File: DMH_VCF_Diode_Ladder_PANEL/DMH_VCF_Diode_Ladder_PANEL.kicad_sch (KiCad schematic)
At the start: 5 parts, among them J0 Panel_GND_Solder_Wire_Pad

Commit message: Designed front panel
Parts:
- added H10: Drive, SynthStuff:Pot_Cutout_Medium, symbol SynthStuff:MountingHole_Pot
- added H11: Resonance, SynthStuff:Pot_Cutout_Medium, symbol SynthStuff:MountingHole_Pot
- added H12: CV 1 Amount, SynthStuff:Pot_Cutout_Tiny, symbol SynthStuff:MountingHole_Pot
- added H13: CV 2 Amount, SynthStuff:Pot_Cutout_Tiny, symbol SynthStuff:MountingHole_Pot
- added H14: LP, SynthStuff:Toggle_Switch_Cutout, symbol SynthStuff:MountingHole_ToggleSwitch
- added H15: BP, SynthStuff:Toggle_Switch_Cutout, symbol SynthStuff:MountingHole_ToggleSwitch
- added H16: HP, SynthStuff:Toggle_Switch_Cutout, symbol SynthStuff:MountingHole_ToggleSwitch
- added H5: Input, SynthStuff:Jack_6.35mm_Cutout_v3, symbol SynthStuff:MountingHole_Jack6.35mm_v2
- added H6: CV 1, SynthStuff:Jack_6.35mm_Cutout_v3, symbol SynthStuff:MountingHole_Jack6.35mm_v2
- added H7: CV 2, SynthStuff:Jack_6.35mm_Cutout_v3, symbol SynthStuff:MountingHole_Jack6.35mm_v2
- added H8: Output, SynthStuff:Jack_6.35mm_Cutout_Output_v6, symbol SynthStuff:MountingHole_Jack6.35mm_Output_v2
- added H9: Cutoff, SynthStuff:Pot_Cutout_Huge_v2, symbol SynthStuff:MountingHole_Pot
- J0: Function Panel GND -> GND
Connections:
- net GND: now also H10.1, H11.1, H12.1, H13.1, H14.1, H15.1, H16.1, H5.1, H6.1, H7.1, H8.1, H9.1

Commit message: Main schematic in progress
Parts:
- added H17: Bus CV Amount, SynthStuff:Pot_Cutout_Tiny, symbol SynthStuff:MountingHole_Pot
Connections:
- net GND: now also H17.1
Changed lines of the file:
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@@
+	)
+	(junction
+		(at 59.69 139.7)
+		(diameter 0)
+		(color 0 0 0 0)
 	)
 	(junction
@@
 	)
 	(junction
+		(at 76.2 114.3)
+		(diameter 0)
+		(color 0 0 0 0)
+	)
+	(junction
 		(at 27.94 269.24)
 		(diameter 0)
@@
 	(wire
 		(pts
+			(xy 59.69 114.3) (xy 59.69 139.7)
+		)
+		(stroke
+			(width 0)
+			(type default)
+		)
+	)
+	(wire
+		(pts
 			(xy 127 130.81) (xy 127 139.7)
 		)
@@
 	(wire
 		(pts
+			(xy 101.6 130.81) (xy 101.6 139.7)
+		)
+		(stroke
+			(width 0)
+			(type default)
+		)
+	)
+	(wire
+		(pts
 			(xy 33.02 269.24) (xy 33.02 273.05)
 		)
@@
 	(wire
 		(pts
+			(xy 76.2 114.3) (xy 59.69 114.3)
+		)
+		(stroke
+			(width 0)
+			(type default)
+		)
+	)
+	(wire
+		(pts
 			(xy 27.94 259.08) (xy 27.94 257.81)
 		)
@@
 		(pts
 			(xy 48.26 269.24) (xy 55.88 269.24)
-		)
-		(stroke
-			(width 0)
-			(type default)
-		)
-	)
-	(wire
-		(pts
-			(xy 101.6 114.3) (xy 101.6 139.7)
 		)
 		(stroke
@@
 					(unit 1)
 				)
+			)
+		)
+	)
+	(symbol
+		(lib_id "SynthStuff:MountingHole_Pot")
+		(at 101.6 128.27 0)
+		(unit 1)
+		(exclude_from_sim yes)
+		(in_bom no)
+		(on_board yes)
+		(dnp no)
+		(fields_autoplaced yes)
+		(property "Reference" "H17"
+			(at 104.14 124.4599 0)
+			(effects
+				(font
+					(size 1.27 1.27)
+				)
+				(justify left)
+			)
+		)
+		(property "Value" "Bus CV Amount"
+			(at 104.14 126.9999 0)
+			(effects
+				(font
+					(size 1.27 1.27)
+				)
+				(justify left)
+			)
+		)
+		(property "Footprint" "SynthStuff:Pot_Cutout_Tiny"
+			(at 101.6 128.27 0)
+			(effects
+				(font
+					(size 1.27 1.27)
+				)
+				(hide yes)
+			)
+		)
+		(property "Datasheet" "~"
+			(at 101.6 128.27 0)
+			(effects
+				(font
+					(size 1.27 1.27)
+				)
+				(hide yes)
+			)
+		)
+		(property "Description" "Pot Mounting Hole"
+			(at 104.14 129.5399 0)
+			(effects
+				(font
+					(size 1.27 1.27)
+				)
+				(justify left)
+			)
+		)
+		(pin "1"
+		)
+		(instances
+			(project "DMH_VCF_Diode_Ladder_PANEL"
+				(path "/a552705f-a9fe-462e-9913-5cfcc08b233c"
+					(reference "H17")
+					(unit 1)
+				)

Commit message: Finished schematic and added Bus CV 2 pot
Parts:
- added H18: CV 2, SynthStuff:Jack_6.35mm_Cutout_v3, symbol SynthStuff:MountingHole_Jack6.35mm_v2
- H13: value CV 2 Amount -> CV 3 Amount
- H17: value Bus CV Amount -> (Bus) CV 2 Amount
- H7: value CV 2 -> CV 3
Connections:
- net GND: now also H18.1
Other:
- moved on the sheet: H5, H6, H7, H8
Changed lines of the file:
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@@
+	)
+	(junction
+		(at 73.66 181.61)
+		(diameter 0)
+		(color 0 0 0 0)
 	)
 	(junction
@@
 	(wire
 		(pts
+			(xy 97.79 181.61) (xy 76.2 181.61)
+		)
+		(stroke
+			(width 0)
+			(type default)
+		)
+	)
+	(wire
+		(pts
 			(xy 127 105.41) (xy 127 114.3)
 		)
@@
 	(wire
 		(pts
+			(xy 97.79 190.5) (xy 97.79 181.61)
+		)
+		(stroke
+			(width 0)
+			(type default)
+		)
+	)
+	(wire
+		(pts
 			(xy 101.6 139.7) (xy 101.6 146.05)
 		)
@@
 	(wire
 		(pts
-			(xy 135.89 190.5) (xy 135.89 181.61)
+			(xy 148.59 190.5) (xy 148.59 181.61)
 		)
 		(stroke
@@
 	(wire
 		(pts
+			(xy 73.66 181.61) (xy 76.2 181.61)
+		)
+		(stroke
+			(width 0)
+			(type default)
+		)
+	)
+	(wire
+		(pts
 			(xy 101.6 92.71) (xy 101.6 114.3)
 		)
@@
 	(wire
 		(pts
+			(xy 148.59 181.61) (xy 135.89 181.61)
+		)
+		(stroke
+			(width 0)
+			(type default)
+		)
+	)
+	(wire
+		(pts
 			(xy 59.69 181.61) (xy 59.69 171.45)
 		)
@@
 	(wire
 		(pts
-			(xy 76.2 181.61) (xy 85.09 181.61)
-		)
-		(stroke
-			(width 0)
-			(type default)
-		)
-	)
-	(wire
-		(pts
 			(xy 55.88 257.81) (xy 55.88 259.08)
 		)
@@
 	(wire
 		(pts
-			(xy 59.69 190.5) (xy 59.69 181.61)
+			(xy 48.26 190.5) (xy 48.26 181.61)
 		)
 		(stroke
@@
 	(wire
 		(pts
-			(xy 110.49 190.5) (xy 110.49 181.61)
+			(xy 123.19 190.5) (xy 123.19 181.61)
 		)
 		(stroke
@@
 	(wire
 		(pts
-			(xy 59.69 181.61) (xy 76.2 181.61)
-		)
-		(stroke
-			(width 0)
-			(type default)
-		)
-	)
-	(wire
-		(pts
-			(xy 110.49 181.61) (xy 135.89 181.61)
+			(xy 59.69 181.61) (xy 73.66 181.61)
+		)
+		(stroke
+			(width 0)
+			(type default)
+		)
+	)
+	(wire
+		(pts
+			(xy 123.19 181.61) (xy 135.89 181.61)
 		)
 		(stroke
@@
 	(wire
 		(pts
-			(xy 85.09 190.5) (xy 85.09 181.61)
+			(xy 48.26 181.61) (xy 59.69 181.61)
+		)
+		(stroke
+			(width 0)
+			(type default)
+		)
+	)
+	(wire
+		(pts
+			(xy 73.66 190.5) (xy 73.66 181.61)
 		)
 		(stroke
@@
 	(symbol
 		(lib_id "SynthStuff:MountingHole_Jack6.35mm_v2")
-		(at 114.3 190.5 0)
+		(at 127 190.5 0)
 		(unit 1)
 		(exclude_from_sim yes)
@@
 		(fields_autoplaced yes)
 		(property "Reference" "H7"
-			(at 116.84 187.9599 0)
-			(effects
-				(font
-					(size 1.27 1.27)
-				)
-				(justify left)
-			)
-		)
-		(property "Value" "CV 2"
-			(at 116.84 190.4999 0)
+			(at 129.54 187.9599 0)
+			(effects
+				(font
+					(size 1.27 1.27)
+				)
+				(justify left)
+			)
+		)
+		(property "Value" "CV 3"
+			(at 129.54 190.4999 0)
 			(effects
 				(font
@@
 		)
 		(property "Footprint" "SynthStuff:Jack_6.35mm_Cutout_v3"
-			(at 114.3 190.5 0)
+			(at 127 190.5 0)
 			(effects
 				(font
@@
 		)
 		(property "Datasheet" "~"
-			(at 114.3 190.5 0)
+			(at 127 190.5 0)
 			(effects
 				(font
@@
 		)
 		(property "Description" "Jack 6.35mm"
-			(at 116.84 193.0399 0)
+			(at 129.54 193.0399 0)
 			(effects
 				(font
@@
 			)
 		)
-		(property "Value" "CV 2 Amount"
+		(property "Value" "CV 3 Amount"
 			(at 129.54 126.9999 0)
 			(effects
@@
 	(symbol
 		(lib_id "SynthStuff:MountingHole_Jack6.35mm_v2")
-		(at 63.5 190.5 0)
+		(at 52.07 190.5 0)
 		(unit 1)
 		(exclude_from_sim yes)
@@
 		(fields_autoplaced yes)
 		(property "Reference" "H5"
-			(at 66.04 187.9599 0)
+			(at 54.61 187.9599 0)
 			(effects
 				(font
@@
 		)
 		(property "Value" "Input"
-			(at 66.04 190.4999 0)
+			(at 54.61 190.4999 0)
 			(effects
 				(font
@@
 		)
 		(property "Footprint" "SynthStuff:Jack_6.35mm_Cutout_v3"
-			(at 63.5 190.5 0)
+			(at 52.07 190.5 0)
 			(effects
 				(font
@@
 		)
 		(property "Datasheet" "~"
-			(at 63.5 190.5 0)
+			(at 52.07 190.5 0)
 			(effects
 				(font
@@
 		)
 		(property "Description" "Jack 6.35mm"
-			(at 66.04 193.0399 0)
+			(at 54.61 193.0399 0)
 			(effects
 				(font
@@
 	(symbol
 		(lib_id "SynthStuff:MountingHole_Jack6.35mm_Output_v2")
-		(at 139.7 190.5 0)
+		(at 152.4 190.5 0)
 		(unit 1)
 		(exclude_from_sim yes)
@@
 		(fields_autoplaced yes)
 		(property "Reference" "H8"
-			(at 142.24 187.9599 0)
+			(at 154.94 187.9599 0)
 			(effects
 				(font
@@
 		)
 		(property "Value" "Output"
-			(at 142.24 190.4999 0)
+			(at 154.94 190.4999 0)
 			(effects
 				(font
@@
 		)
 		(property "Footprint" "SynthStuff:Jack_6.35mm_Cutout_Output_v6"
-			(at 139.7 190.5 0)
+			(at 152.4 190.5 0)
 			(effects
 				(font
@@
 		)
 		(property "Datasheet" "~"
-			(at 139.7 190.5 0)
+			(at 152.4 190.5 0)
 			(effects
 				(font
@@
 		)
 		(property "Description" "Jack 6.35mm Output"
-			(at 142.24 193.0399 0)
+			(at 154.94 193.0399 0)
 			(effects
 				(font
@@
 			)
 		)
-		(property "Value" "Bus CV Amount"
+		(property "Value" "(Bus) CV 2 Amount"
 			(at 104.14 126.9999 0)
 			(effects
@@
 	)
 	(symbol
+		(lib_id "SynthStuff:MountingHole_Jack6.35mm_v2")
+		(at 101.6 190.5 0)
+		(unit 1)
+		(exclude_from_sim yes)
+		(in_bom no)
+		(on_board yes)
+		(dnp no)
+		(fields_autoplaced yes)
+		(property "Reference" "H18"
+			(at 104.14 187.9599 0)
+			(effects
+				(font
+					(size 1.27 1.27)
+				)
+				(justify left)
+			)
+		)
+		(property "Value" "CV 2"
+			(at 104.14 190.4999 0)
+			(effects
+				(font
+					(size 1.27 1.27)
+				)
+				(justify left)
+			)
+		)
+		(property "Footprint" "SynthStuff:Jack_6.35mm_Cutout_v3"
+			(at 101.6 190.5 0)
+			(effects
+				(font
+					(size 1.27 1.27)
+				)
+				(hide yes)
+			)
+		)
+		(property "Datasheet" "~"
+			(at 101.6 190.5 0)
+			(effects
+				(font
+					(size 1.27 1.27)
+				)
+				(hide yes)
+			)
+		)
+		(property "Description" "Jack 6.35mm"
+			(at 104.14 193.0399 0)
+			(effects
+				(font
+					(size 1.27 1.27)
+				)
+				(justify left)
+			)
+		)
+		(pin "1"
+		)
+		(instances
+			(project "DMH_VCF_Diode_Ladder_PANEL"
+				(path "/a552705f-a9fe-462e-9913-5cfcc08b233c"
+					(reference "H18")
+					(unit 1)
+				)
+			)
+		)
+	)
+	(symbol
 		(lib_id "SynthStuff:MountingHole_Pot")
 		(at 76.2 102.87 0)
@@
 	(symbol
 		(lib_id "SynthStuff:MountingHole_Jack6.35mm_v2")
-		(at 88.9 190.5 0)
+		(at 77.47 190.5 0)
 		(unit 1)
 		(exclude_from_sim yes)
@@
 		(fields_autoplaced yes)
 		(property "Reference" "H6"
-			(at 91.44 187.9599 0)
+			(at 80.01 187.9599 0)
 			(effects
 				(font
@@
 		)
 		(property "Value" "CV 1"
-			(at 91.44 190.4999 0)
+			(at 80.01 190.4999 0)
 			(effects
 				(font
@@
 		)
 		(property "Footprint" "SynthStuff:Jack_6.35mm_Cutout_v3"
-			(at 88.9 190.5 0)
+			(at 77.47 190.5 0)
 			(effects
 				(font
@@
 		)
 		(property "Datasheet" "~"
-			(at 88.9 190.5 0)
+			(at 77.47 190.5 0)
 			(effects
 				(font
@@
 		)
 		(property "Description" "Jack 6.35mm"
-			(at 91.44 193.0399 0)
-			(effects
-				(font
+			(at 80.01 193.0399 0)
+			(effects
+				(font

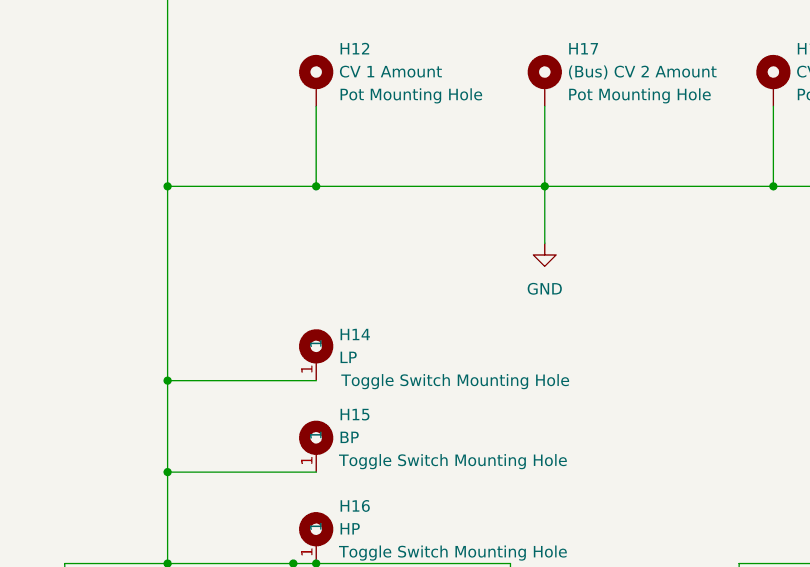
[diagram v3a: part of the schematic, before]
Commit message: Added Bus CV On Off switch
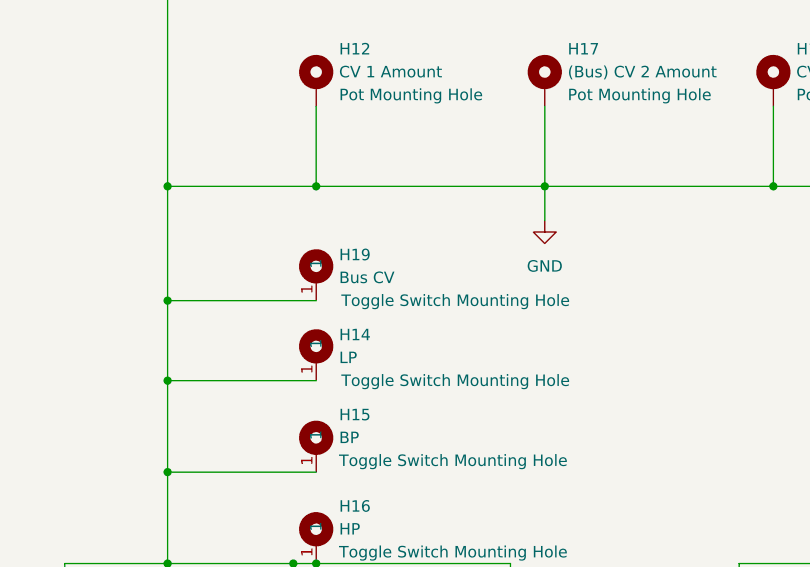
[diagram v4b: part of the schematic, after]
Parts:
- added H19: Bus CV, SynthStuff:Toggle_Switch_Cutout, symbol SynthStuff:MountingHole_ToggleSwitch
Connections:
- net GND: now also H19.1
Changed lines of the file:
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@@
+	)
+	(junction
+		(at 59.69 152.4)
+		(diameter 0)
+		(color 0 0 0 0)
 	)
 	(junction
@@
 	(wire
 		(pts
-			(xy 59.69 161.29) (xy 59.69 139.7)
+			(xy 59.69 161.29) (xy 59.69 152.4)
 		)
 		(stroke
@@
 	(wire
 		(pts
-			(xy 101.6 139.7) (xy 101.6 146.05)
+			(xy 101.6 139.7) (xy 101.6 143.51)
 		)
 		(stroke
@@
 		(pts
 			(xy 73.66 181.61) (xy 76.2 181.61)
+		)
+		(stroke
+			(width 0)
+			(type default)
+		)
+	)
+	(wire
+		(pts
+			(xy 59.69 152.4) (xy 76.2 152.4)
+		)
+		(stroke
+			(width 0)
+			(type default)
+		)
+	)
+	(wire
+		(pts
+			(xy 59.69 152.4) (xy 59.69 139.7)
 		)
 		(stroke
@@
 	(symbol
 		(lib_id "power:GND")
-		(at 101.6 146.05 0)
+		(at 101.6 143.51 0)
 		(unit 1)
 		(exclude_from_sim no)
@@
 		(fields_autoplaced yes)
 		(property "Reference" "#PWR02"
-			(at 101.6 152.4 0)
+			(at 101.6 149.86 0)
 			(effects
 				(font
@@
 		)
 		(property "Value" "GND"
-			(at 101.6 151.13 0)
+			(at 101.6 148.59 0)
 			(effects
 				(font
@@
 		)
 		(property "Footprint" ""
-			(at 101.6 146.05 0)
+			(at 101.6 143.51 0)
 			(effects
 				(font
@@
 		)
 		(property "Datasheet" ""
-			(at 101.6 146.05 0)
+			(at 101.6 143.51 0)
 			(effects
 				(font
@@
 		)
 		(property "Description" "Power symbol creates a global label with name \"GND\" , ground"
-			(at 101.6 146.05 0)
+			(at 101.6 143.51 0)
 			(effects
 				(font
@@
 					(unit 1)
 				)
+			)
+		)
+	)
+	(symbol
+		(lib_name "MountingHole_ToggleSwitch_1")
+		(lib_id "SynthStuff:MountingHole_ToggleSwitch")
+		(at 76.2 148.59 0)
+		(unit 1)
+		(exclude_from_sim yes)
+		(in_bom no)
+		(on_board yes)
+		(dnp no)
+		(property "Reference" "H19"
+			(at 78.74 147.3199 0)
+			(effects
+				(font
+					(size 1.27 1.27)
+				)
+				(justify left)
+			)
+		)
+		(property "Value" "Bus CV"
+			(at 78.74 149.8599 0)
+			(effects
+				(font
+					(size 1.27 1.27)
+				)
+				(justify left)
+			)
+		)
+		(property "Footprint" "SynthStuff:Toggle_Switch_Cutout"
+			(at 76.2 148.59 0)
+			(effects
+				(font
+					(size 1.27 1.27)
+				)
+				(hide yes)
+			)
+		)
+		(property "Datasheet" "~"
+			(at 76.2 148.59 0)
+			(effects
+				(font
+					(size 1.27 1.27)
+				)
+				(hide yes)
+			)
+		)
+		(property "Description" "Toggle Switch Mounting Hole"
+			(at 78.994 152.4 0)
+			(effects
+				(font
+					(size 1.27 1.27)
+				)
+				(justify left)
+			)
+		)
+		(property "Function" "Bus CV"
+			(at 80.01 152.146 0)
+			(effects
+				(font
+					(size 1.27 1.27)
+					(thickness 0.1588)
+				)
+				(hide yes)
+			)
+		)
+		(pin "1"
+		)
+		(instances
+			(project "DMH_VCF_Diode_Ladder_PANEL"
+				(path "/a552705f-a9fe-462e-9913-5cfcc08b233c"
+					(reference "H19")
+					(unit 1)
+				)
